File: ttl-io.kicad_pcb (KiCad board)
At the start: 4 copper layers, 47.2 x 30 mm, 56 parts, among them J1 PMOD, J2 430451628, U1 SN74LVC1G16DBVR, U2 SN74LVC1G16DBVR, U3 SN74LVC1G16DBVR, U4 SN74LVC1G16DBVR, U5 SN74AC14PWR, U6 SN74LVC3G34DCT, U7 SN74LVC3G34DCT, U8 SN74LVC3G34DCT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

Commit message: Updated part values/#s
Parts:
- R10, R12, R14, R16: value 50k -> 49.9k
- R17, R18, R19, R20, R21, R22, R23, R24, R25, R26, R27, R28: value 143 -> 10

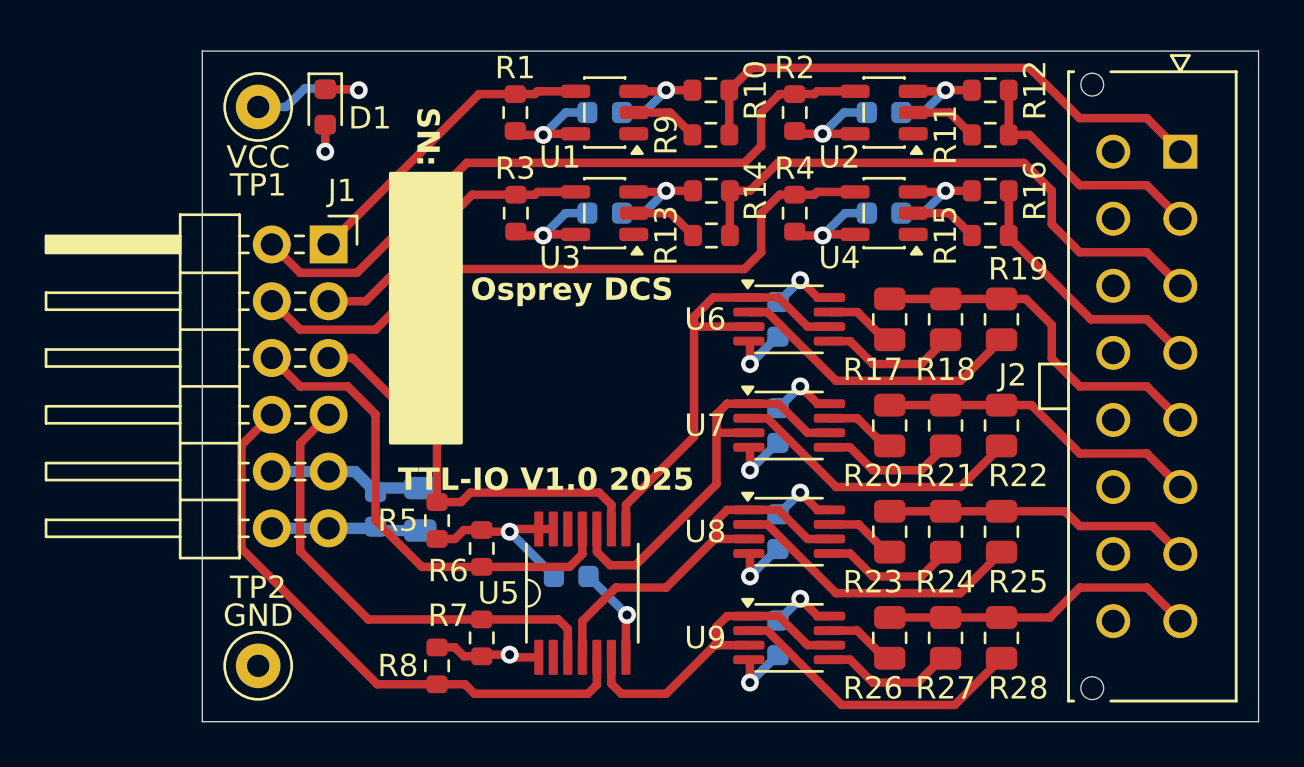
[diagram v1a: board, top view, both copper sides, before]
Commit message: Updated sch notes and part info, ready for fab
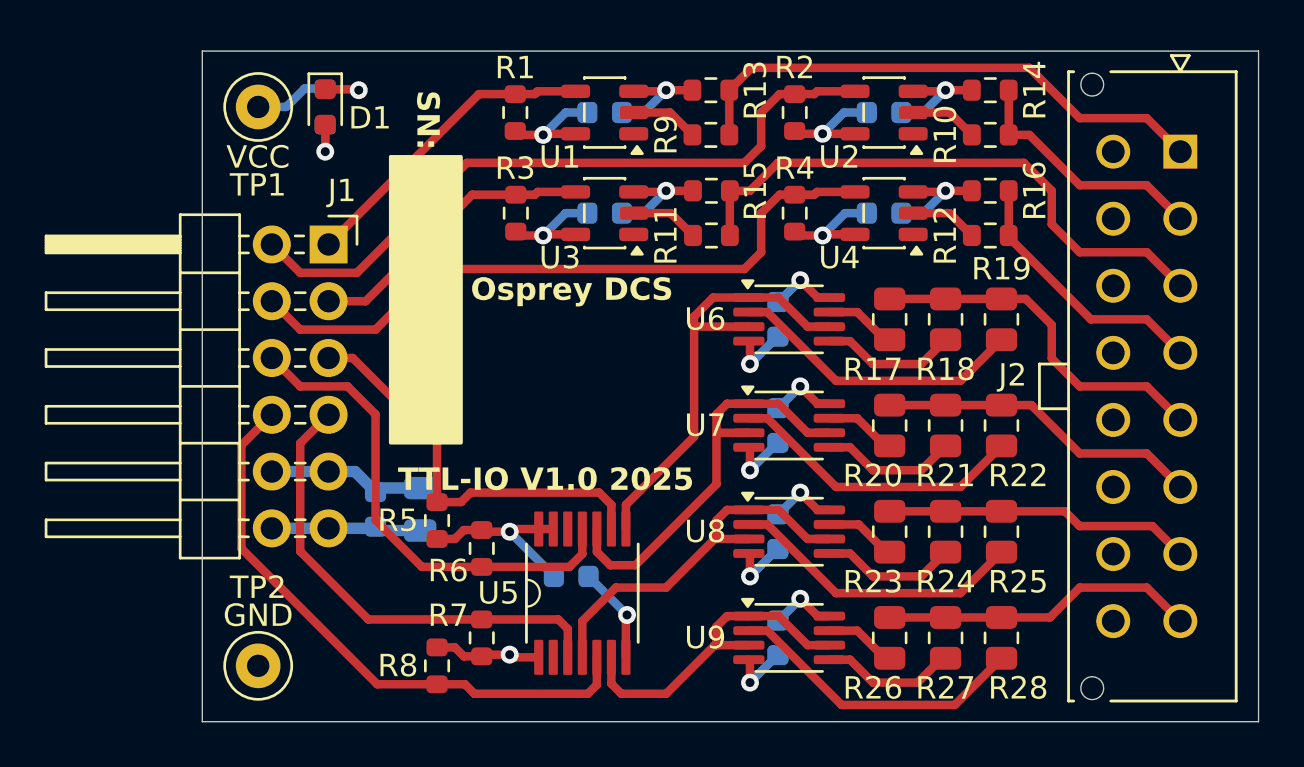
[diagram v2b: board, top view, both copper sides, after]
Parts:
- TP1: value TestPoint -> TestPointRed
- TP2: value TestPoint -> TestPointBlack
- renumbered R11 to R10, R13 to R11, R15 to R12, R10 to R13, R12 to R14, R14 to R15
